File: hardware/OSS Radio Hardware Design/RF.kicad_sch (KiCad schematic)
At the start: 9 parts, among them U4 SI4468-A2A-IM, Y2 RTX-104EF3C-S-30.000-TR

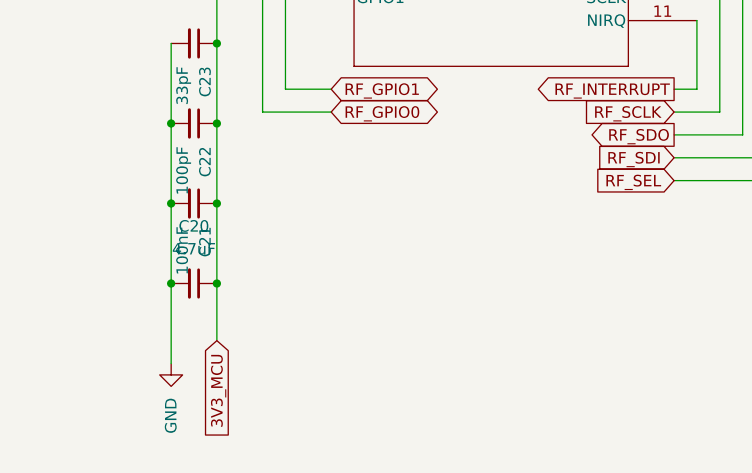
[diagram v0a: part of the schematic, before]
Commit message: schematic for sd card, external flash, working on audio amp
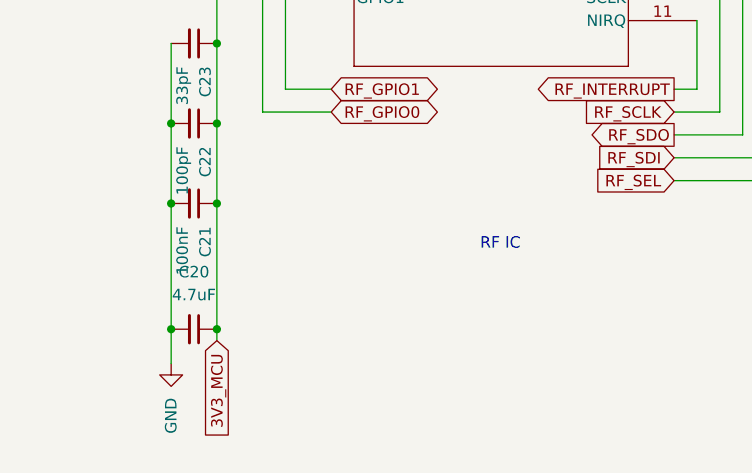
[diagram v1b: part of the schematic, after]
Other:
- note added: "RF IC"
- moved on the sheet: C20
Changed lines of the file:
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@@
 	(generator_version "9.0")
 	(paper "A4")
+	(text "RF IC\n"
+		(exclude_from_sim no)
+		(at 164.846 130.302 0)
+		(effects
+			(font
+				(size 1.27 1.27)
+			)
+		)
+	)
 	(junction
 		(at 133.35 116.84)
@@
 	)
 	(junction
-		(at 128.27 134.62)
-		(diameter 0)
-		(color 0 0 0 0)
-	)
-	(junction
 		(at 220.98 87.63)
 		(diameter 0)
@@
 	)
 	(junction
-		(at 133.35 134.62)
+		(at 128.27 139.7)
+		(diameter 0)
+		(color 0 0 0 0)
+	)
+	(junction
+		(at 133.35 139.7)
 		(diameter 0)
 		(color 0 0 0 0)
@@
 	(wire
 		(pts
-			(xy 128.27 134.62) (xy 128.27 143.51)
+			(xy 128.27 125.73) (xy 128.27 139.7)
 		)
 		(stroke
@@
 	(wire
 		(pts
-			(xy 128.27 125.73) (xy 128.27 134.62)
-		)
-		(stroke
-			(width 0)
-			(type default)
-		)
-	)
-	(wire
-		(pts
-			(xy 133.35 134.62) (xy 133.35 140.97)
-		)
-		(stroke
-			(width 0)
-			(type default)
-		)
-	)
-	(wire
-		(pts
 			(xy 186.69 90.17) (xy 194.31 90.17)
 		)
@@
 	(wire
 		(pts
+			(xy 133.35 125.73) (xy 133.35 139.7)
+		)
+		(stroke
+			(width 0)
+			(type default)
+		)
+	)
+	(wire
+		(pts
 			(xy 140.97 92.71) (xy 138.43 92.71)
 		)
@@
 	(wire
 		(pts
-			(xy 133.35 125.73) (xy 133.35 134.62)
-		)
-		(stroke
-			(width 0)
-			(type default)
-		)
-	)
-	(wire
-		(pts
 			(xy 113.03 82.55) (xy 140.97 82.55)
 		)
@@
 	(wire
 		(pts
+			(xy 128.27 139.7) (xy 128.27 143.51)
+		)
+		(stroke
+			(width 0)
+			(type default)
+		)
+	)
+	(wire
+		(pts
 			(xy 138.43 92.71) (xy 138.43 97.79)
 		)
@@
 		(pts
 			(xy 191.77 118.11) (xy 184.15 118.11)
+		)
+		(stroke
+			(width 0)
+			(type default)
+		)
+	)
+	(wire
+		(pts
+			(xy 133.35 139.7) (xy 133.35 140.97)
 		)
 		(stroke
@@
 	(symbol
 		(lib_id "Device:C_Small")
-		(at 130.81 134.62 270)
+		(at 130.81 139.7 270)
 		(unit 1)
 		(exclude_from_sim no)
@@
 		(fields_autoplaced yes)
 		(property "Reference" "C20"
-			(at 130.8036 128.27 90)
+			(at 130.8036 133.35 90)
 			(effects
 				(font
@@
 		)
 		(property "Value" "4.7uF"
-			(at 130.8036 130.81 90)
+			(at 130.8036 135.89 90)
 			(effects
 				(font
@@
 		)
 		(property "Footprint" ""
-			(at 130.81 134.62 0)
+			(at 130.81 139.7 0)
 			(effects
 				(font
@@
 		)
 		(property "Datasheet" "~"
-			(at 130.81 134.62 0)
+			(at 130.81 139.7 0)
 			(effects
 				(font
@@
 		)
 		(property "Description" "Unpolarized capacitor, small symbol"
-			(at 130.81 134.62 0)
-			(effects
-				(font
+			(at 130.81 139.7 0)
+			(effects
+				(font

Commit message: BOM consolidation
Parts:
- C20: value 4.7uF -> 4.7u
- C21: value 100nF -> 100n
- C22, C25: value 100pF -> 100p
- C23: value 33pF -> 15p
- C24: value 10nF -> 10n
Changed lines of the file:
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@@
 	(text "RF IC\n"
 		(exclude_from_sim no)
-		(at 164.846 130.302 0)
+		(at 163.576 128.778 0)
 		(effects
 			(font
@@
 			)
 		)
-		(property "Value" "10nF"
+		(property "Value" "10n"
 			(at 223.52 92.7162 0)
 			(effects
@@
 			)
 		)
-		(property "Value" "100nF"
+		(property "Value" "100n"
 			(at 129.5338 128.27 0)
 			(effects
@@
 		(on_board yes)
 		(dnp no)
-		(fields_autoplaced yes)
 		(property "Reference" "C20"
-			(at 130.8036 133.35 90)
-			(effects
-				(font
-					(size 1.27 1.27)
-				)
-			)
-		)
-		(property "Value" "4.7uF"
-			(at 130.8036 135.89 90)
+			(at 130.81 134.62 90)
+			(effects
+				(font
+					(size 1.27 1.27)
+				)
+			)
+		)
+		(property "Value" "4.7u"
+			(at 130.81 136.906 90)
 			(effects
 				(font
@@
 			)
 		)
-		(property "Value" "100pF"
+		(property "Value" "100p"
 			(at 200.914 91.44 90)
 			(effects
@@
 			)
 		)
-		(property "Value" "33pF"
+		(property "Value" "15p"
 			(at 129.5338 110.49 0)
 			(effects
@@
 			)
 		)
-		(property "Value" "100pF"
+		(property "Value" "100p"
 			(at 129.5338 119.38 0)
 			(effects

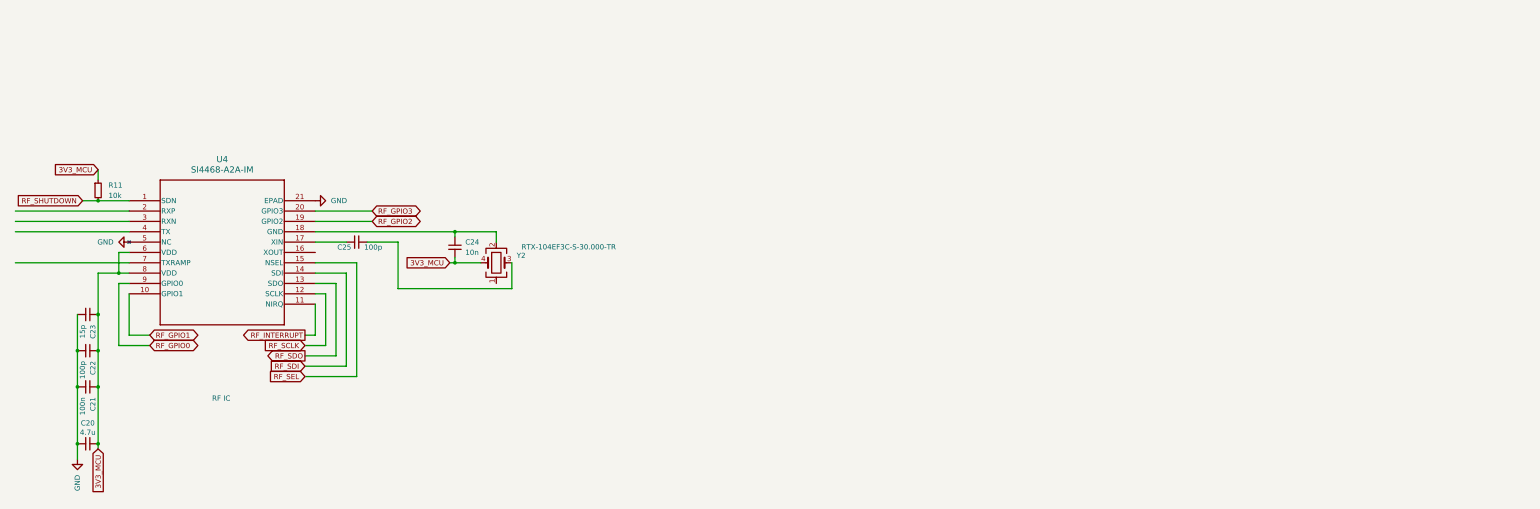
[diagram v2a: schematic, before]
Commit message: throwout Si4468, CC1120 is my friend now. FM has better support apparently
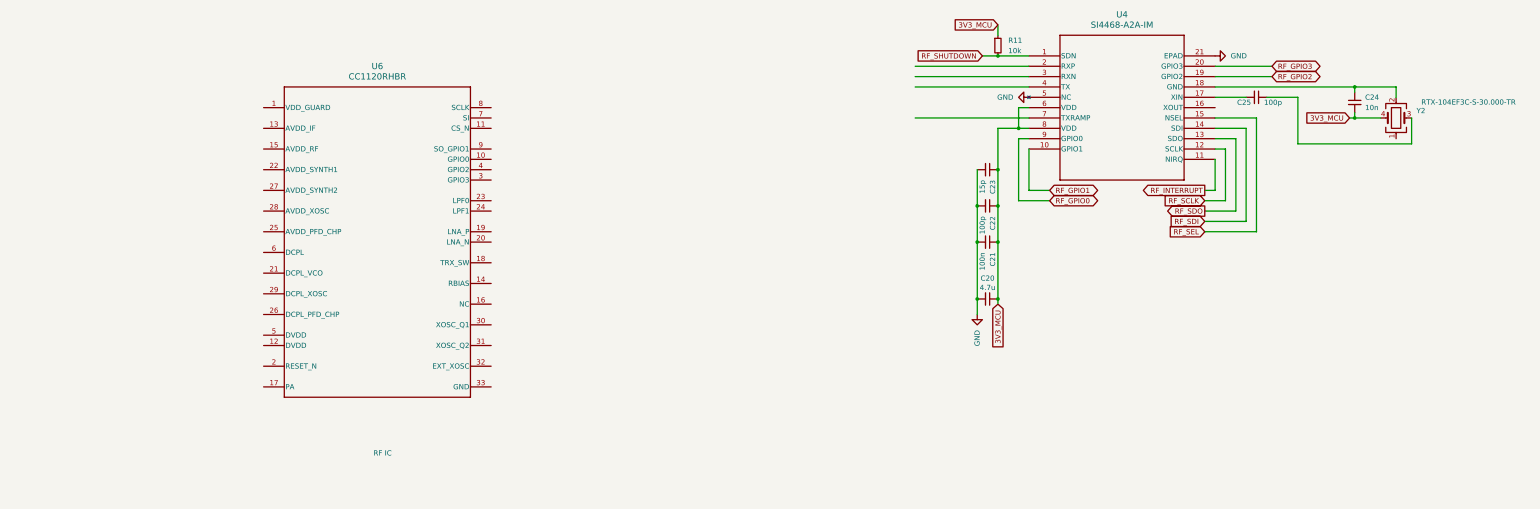
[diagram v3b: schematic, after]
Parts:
- added U6: CC1120RHBR, RHB0032E, symbol CC1120:CC1120RHBR
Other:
- moved on the sheet: C20, C21, C22, C23, C24, C25, R11, U4, Y2

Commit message: added ESD diodes, MARS resistor, Charge LED, Status LED
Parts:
- added C100, C44, C45, C46, C83, C84, C85, C86, C87, C88, C89, C91, C92, C95: 100n, symbol Device:C_Small
- added C93: 1.8n, symbol Device:C_Small
- added C94: 1n, symbol Device:C_Small
- added R41: 56k 1%, symbol Device:R_Small
- added R48: 5k1, symbol Device:R_Small
- added Y3: END4263D-32M, Oscillator:Oscillator_SMD_SeikoEpson_TG2520SMN-xxx-xxxxxx-4Pin_2.5x2.0mm, symbol Oscillator:TG2520SMN-xx.xxxxxxMhz-xxxxNM
- C20, C21, C22, C23, C25, R11, U4, Y2: now not fitted
- C24: value 10n -> 100n; now not fitted
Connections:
- net 3V3_MCU: now also U6.1 (VDD_GUARD), U6.12 (DVDD), U6.13 (AVDD_IF), U6.15 (AVDD_RF), U6.22 (AVDD_SYNTH1), U6.25 (AVDD_PFD_CHP), U6.27 (AVDD_SYNTH2), U6.28 (AVDD_XOSC), U6.5 (DVDD), C44.1, C45.1, C46.1, C83.1, C84.1, C85.1, C86.1, C87.1, C88.1, C95.2, R48.1, Y3.4 (Vcc)
- net GND: now also U6.30 (XOSC_Q1), U6.33 (GND), C100.2, C44.2, C45.2, C46.2, C83.2, C84.2, C85.2, C86.2, C87.2, C88.2, C89.2, C91.2, C92.2, C95.1, R41.2
- net RF_GPIO0: now also U6.10 (GPIO0)
- net RF_GPIO2: now also U6.4 (GPIO2)
- net RF_GPIO3: now also U6.3 (GPIO3)
- net RF_SCLK: now also U6.8 (SCLK)
- net RF_SDI: now also U6.7 (SI)
- net RF_SDO: now also U6.9 (SO_GPIO1)
- net RF_SEL: now also U6.11 (CS_N)
- net at U6.14 (RBIAS): now also R41.1
- net at U6.2 (RESET_N): now also R48.2
- net at U6.21 (DCPL_VCO): now also C100.1
- net at U6.23 (LPF0): now also C93.2
- net at U6.24 (LPF1): now also C93.1
- net at U6.26 (DCPL_PFD_CHP): now also C92.1
- net at U6.29 (DCPL_XOSC): now also C91.1
- net at U6.32 (EXT_XOSC): now also C94.2
- net at U6.6 (DCPL): now also C89.1
- new net: C94.1, Y3.3 (OUT)
- no-connect marks 0 -> 2
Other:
- moved on the sheet: U6

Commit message: working on fooprints
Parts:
- C100, C44, C45, C46, C83, C84, C85, C86, C87, C88, C89, C91, C92, C95: footprint (none) -> Capacitor_SMD:C_0402_1005Metric_Pad0.74x0.62mm_HandSolder
- C93, C94: footprint (none) -> Capacitor_SMD:C_0603_1608Metric_Pad1.08x0.95mm_HandSolder
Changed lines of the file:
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@@
 			)
 		)
-		(property "Footprint" ""
+		(property "Footprint" "Capacitor_SMD:C_0402_1005Metric_Pad0.74x0.62mm_HandSolder"
 			(at 25.4 62.23 0)
 			(effects
@@
 			)
 		)
-		(property "Footprint" ""
+		(property "Footprint" "Capacitor_SMD:C_0402_1005Metric_Pad0.74x0.62mm_HandSolder"
 			(at 25.4 46.99 0)
 			(effects
@@
 			)
 		)
-		(property "Footprint" ""
+		(property "Footprint" "Capacitor_SMD:C_0402_1005Metric_Pad0.74x0.62mm_HandSolder"
 			(at 25.4 77.47 0)
 			(effects
@@
 			)
 		)
-		(property "Footprint" ""
+		(property "Footprint" "Capacitor_SMD:C_0402_1005Metric_Pad0.74x0.62mm_HandSolder"
 			(at 25.4 101.6 0)
 			(effects
@@
 			)
 		)
-		(property "Footprint" ""
+		(property "Footprint" "Capacitor_SMD:C_0603_1608Metric_Pad1.08x0.95mm_HandSolder"
 			(at 95.25 105.41 0)
 			(effects
@@
 			)
 		)
-		(property "Footprint" ""
+		(property "Footprint" "Capacitor_SMD:C_0402_1005Metric_Pad0.74x0.62mm_HandSolder"
 			(at 25.4 67.31 0)
 			(effects
@@
 			)
 		)
-		(property "Footprint" ""
+		(property "Footprint" "Capacitor_SMD:C_0402_1005Metric_Pad0.74x0.62mm_HandSolder"
 			(at 25.4 97.79 0)
 			(effects
@@
 			)
 		)
-		(property "Footprint" ""
+		(property "Footprint" "Capacitor_SMD:C_0402_1005Metric_Pad0.74x0.62mm_HandSolder"
 			(at 25.4 92.71 0)
 			(effects
@@
 			)
 		)
-		(property "Footprint" ""
+		(property "Footprint" "Capacitor_SMD:C_0402_1005Metric_Pad0.74x0.62mm_HandSolder"
 			(at 25.4 52.07 0)
 			(effects
@@
 			)
 		)
-		(property "Footprint" ""
+		(property "Footprint" "Capacitor_SMD:C_0402_1005Metric_Pad0.74x0.62mm_HandSolder"
 			(at 25.4 87.63 0)
 			(effects
@@
 			)
 		)
-		(property "Footprint" ""
+		(property "Footprint" "Capacitor_SMD:C_0402_1005Metric_Pad0.74x0.62mm_HandSolder"
 			(at 25.4 57.15 0)
 			(effects
@@
 			)
 		)
-		(property "Footprint" ""
+		(property "Footprint" "Capacitor_SMD:C_0402_1005Metric_Pad0.74x0.62mm_HandSolder"
 			(at 116.84 105.41 0)
 			(effects
@@
 			)
 		)
-		(property "Footprint" ""
+		(property "Footprint" "Capacitor_SMD:C_0402_1005Metric_Pad0.74x0.62mm_HandSolder"
 			(at 25.4 72.39 0)
 			(effects
@@
 			)
 		)
-		(property "Footprint" ""
+		(property "Footprint" "Capacitor_SMD:C_0603_1608Metric_Pad1.08x0.95mm_HandSolder"
 			(at 93.98 64.77 0)
 			(effects
@@
 			)
 		)
-		(property "Footprint" ""
+		(property "Footprint" "Capacitor_SMD:C_0402_1005Metric_Pad0.74x0.62mm_HandSolder"
 			(at 25.4 82.55 0)
 			(effects
@@
 			)
 		)
-		(property "Footprint" ""
+		(property "Footprint" "Capacitor_SMD:C_0402_1005Metric_Pad0.74x0.62mm_HandSolder"
 			(at 25.4 41.91 0)
 			(effects
